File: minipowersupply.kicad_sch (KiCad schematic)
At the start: 43 parts, among them J1 Conn_01x08_Female, J2 Conn_01x08_Female, J3 Conn_01x03_Female, J4 Conn_01x08_Female, J5 Conn_01x03_Female, J6 Conn_01x08_Female, J7 Conn_01x03_Female, J8 Conn_01x02_Female, J9 Conn_01x02_Female, Q1 BC817, U1 LM7805_TO220, U15 LT1084-3.3, U2 LM317L_TO92, U3 LM337L_TO92, U4 CD74HC4067SM

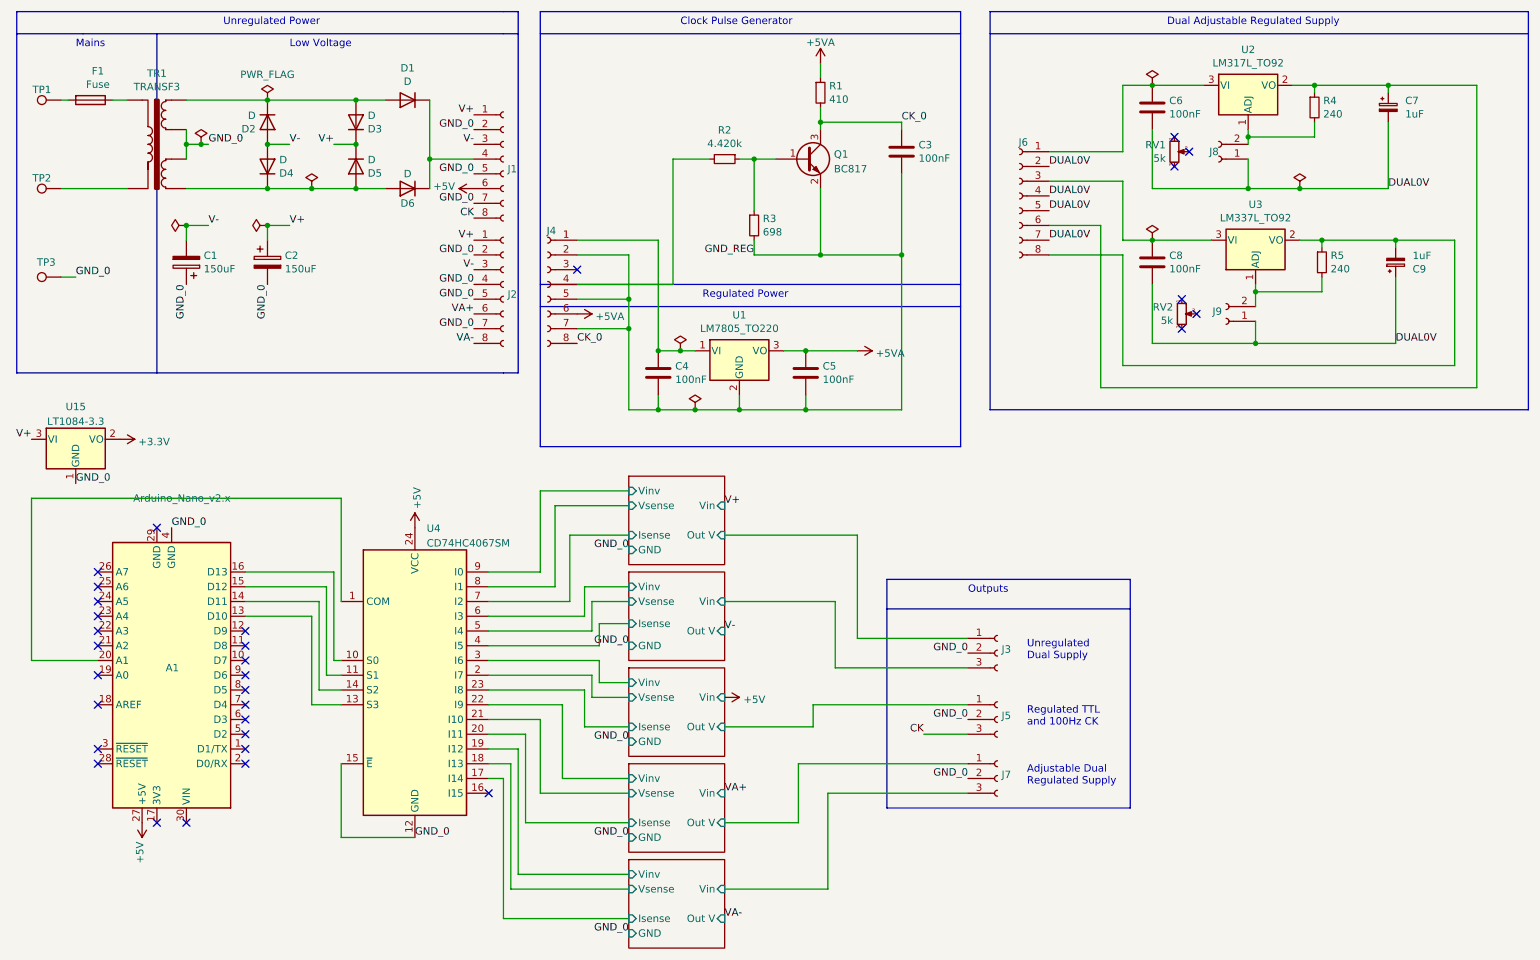
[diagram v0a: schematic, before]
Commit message: Reduced to simplest layout structure in readiness for PCBWay production
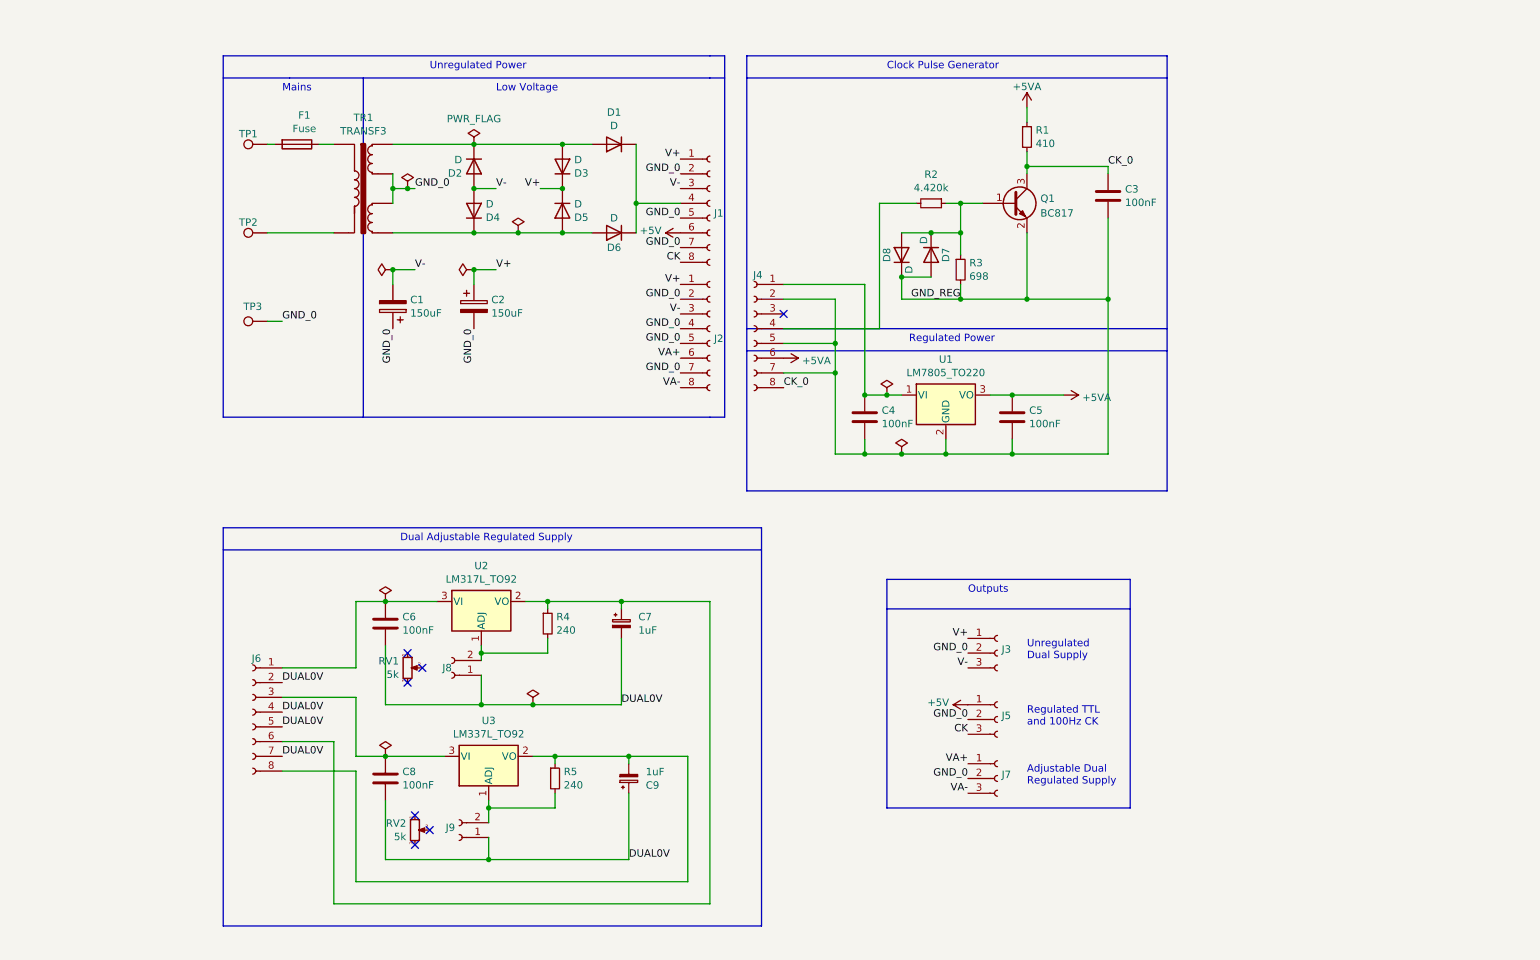
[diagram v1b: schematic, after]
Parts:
- removed A1: Arduino_Nano_v2.x, Module:Arduino_Nano, symbol MCU_Module:Arduino_Nano_v2.x
- removed U15: LT1084-3.3, symbol Regulator_Linear:LT1084-3.3
- removed U4: CD74HC4067SM, Package_SO:SSOP-24_5.3x8.2mm_P0.65mm, symbol 74xx:CD74HC4067SM
- added D7, D8: D, Diode_THT:D_T-1_P5.08mm_Horizontal, symbol Device:D
- TP1, TP2, TP3: footprint TestPoint:TestPoint_THTPad_4.0x4.0mm_Drill2.0mm -> TestPoint:TestPoint_THTPad_2.5x2.5mm_Drill1.2mm
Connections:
- net Curent and Volt4/Out V is gone; now on net V+: J3.1 (Pin_1)
- net Curent and Volt5/Vin is gone; now on net V-: J3.3 (Pin_3)
- net Curent and Volt6/Out V is gone; now on net +5V: J5.1 (Pin_1)
- net Curent and Volt7/Out V is gone; now on net VA+: J7.1 (Pin_1)
- net Curent and Volt8/Vin is gone; now on net VA-: J7.3 (Pin_3)
- net GND_REG: now also D7.1 (K), D8.2 (A)
- net at Q1.1 (B), R2.1, R3.1: now also D7.2 (A), D8.1 (K)
- no-connect marks 31 -> 7
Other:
- removed sheet Curent and Volt4
- removed sheet Curent and Volt5
- removed sheet Curent and Volt6
- removed sheet Curent and Volt7
- removed sheet Curent and Volt8
- moved on the sheet: C1, C2, C3, C4, C5, C6, C7, C8, C9, D1, D2, D3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
